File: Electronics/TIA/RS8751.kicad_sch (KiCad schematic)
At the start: 16 parts

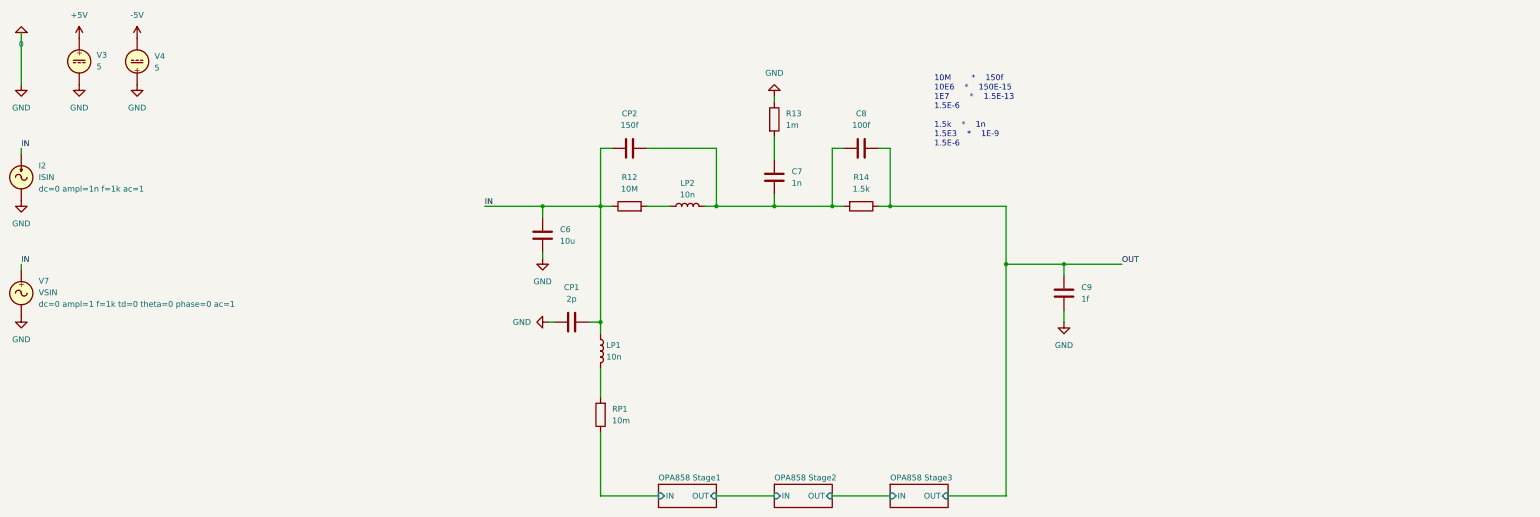
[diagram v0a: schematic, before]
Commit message: Create simulation for RS8751
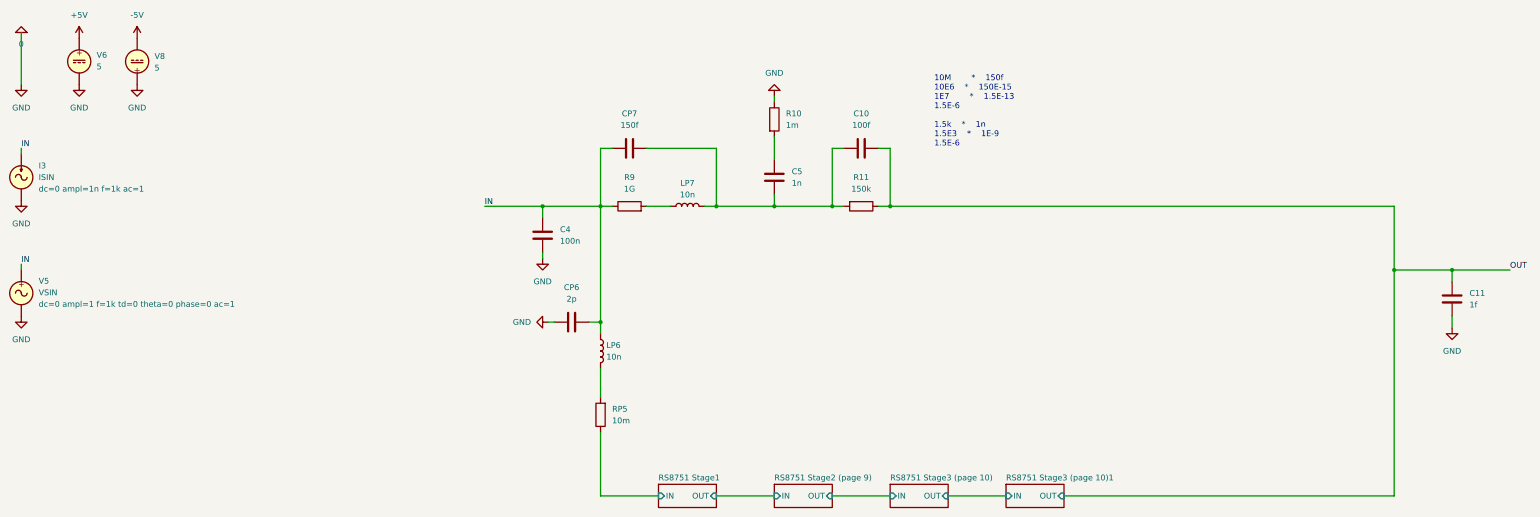
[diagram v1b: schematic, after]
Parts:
- removed C6: 10u, symbol Device:C
- removed C7: 1n, symbol Device:C
- removed C8: 100f, symbol Device:C
- removed C9: 1f, symbol Device:C
- removed CP1: 2p, symbol Device:C
- removed CP2: 150f, symbol Device:C
- removed I2: ISIN, symbol Simulation_SPICE:ISIN
- removed LP1, LP2: 10n, symbol Device:L
- removed R12: 10M, symbol Device:R
- removed R13: 1m, symbol Device:R
- removed R14: 1.5k, symbol Device:R
- removed RP1: 10m, symbol Device:R
- removed V3, V4: 5, symbol Simulation_SPICE:VDC
- removed V7: VSIN, symbol Simulation_SPICE:VSIN
- added C10: 100f, symbol Device:C
- added C11: 1f, symbol Device:C
- added C4: 100n, symbol Device:C
- added C5: 1n, symbol Device:C
- added CP6: 2p, symbol Device:C
- added CP7: 150f, symbol Device:C
- added I3: ISIN, symbol Simulation_SPICE:ISIN
- added LP6, LP7: 10n, symbol Device:L
- added R10: 1m, symbol Device:R
- added R11: 150k, symbol Device:R
- added R9: 1G, symbol Device:R
- added RP5: 10m, symbol Device:R
- added V5: VSIN, symbol Simulation_SPICE:VSIN
- added V6, V8: 5, symbol Simulation_SPICE:VDC
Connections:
- net +5V: now also V6.1
- net -5V: now also V8.2
- net 0: now also C11.2, C4.2, CP6.2, I3.2, R10.1, V5.2, V6.2, V8.1
- net IN: now also C4.1, CP6.1, CP7.1, I3.1, LP6.1, R9.1, V5.1
- net OUT: now also C10.2, C11.1, R11.1
- new net: C5.1, R10.2
- new net: LP6.2, RP5.2
- new net: LP7.1, R9.2
- new net: C10.1, C5.2, CP7.2, LP7.2, R11.2
- new net RS8751 Stage1/IN: RP5.1
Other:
- removed sheet OPA858 Stage1
- removed sheet OPA858 Stage2
- removed sheet OPA858 Stage3
- added sheet RS8751 Stage1 (OPA858 Stage.kicad_sch)
- added sheet RS8751 Stage2 (page 9) (OPA858 Stage.kicad_sch)
- added sheet RS8751 Stage3 (page 10) (OPA858 Stage.kicad_sch)
- added sheet RS8751 Stage3 (page 10)1 (OPA858 Stage.kicad_sch)

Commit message: Mess around with the TIA simulation
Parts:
- C4: value 100n -> 10n
- CP7: value 150f -> 1p
- R11: value 150k -> 10k
- R9: value 1G -> 10M
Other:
- removed sheet RS8751 Stage3 (page 10)1
- note added: "P in CP, RP and LP is for parasitics, not actual components."
- moved on the sheet: C10, C11, C4, C5, CP6, CP7, LP6, LP7, R10, R11, R9, RP5
